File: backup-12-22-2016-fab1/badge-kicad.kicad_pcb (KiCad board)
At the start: 4 copper layers, 153.5 x 153.5 mm, 100 parts, among them J2 JTAG, P1 TM1000, P2 CONN_02X20, P3 FTDI BACKUP, P4 USB_OTG, Q1 MNBT3904, SW1 SW_PUSH, U1 WS2812B, U10 WS2812B, U11 WS2812B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

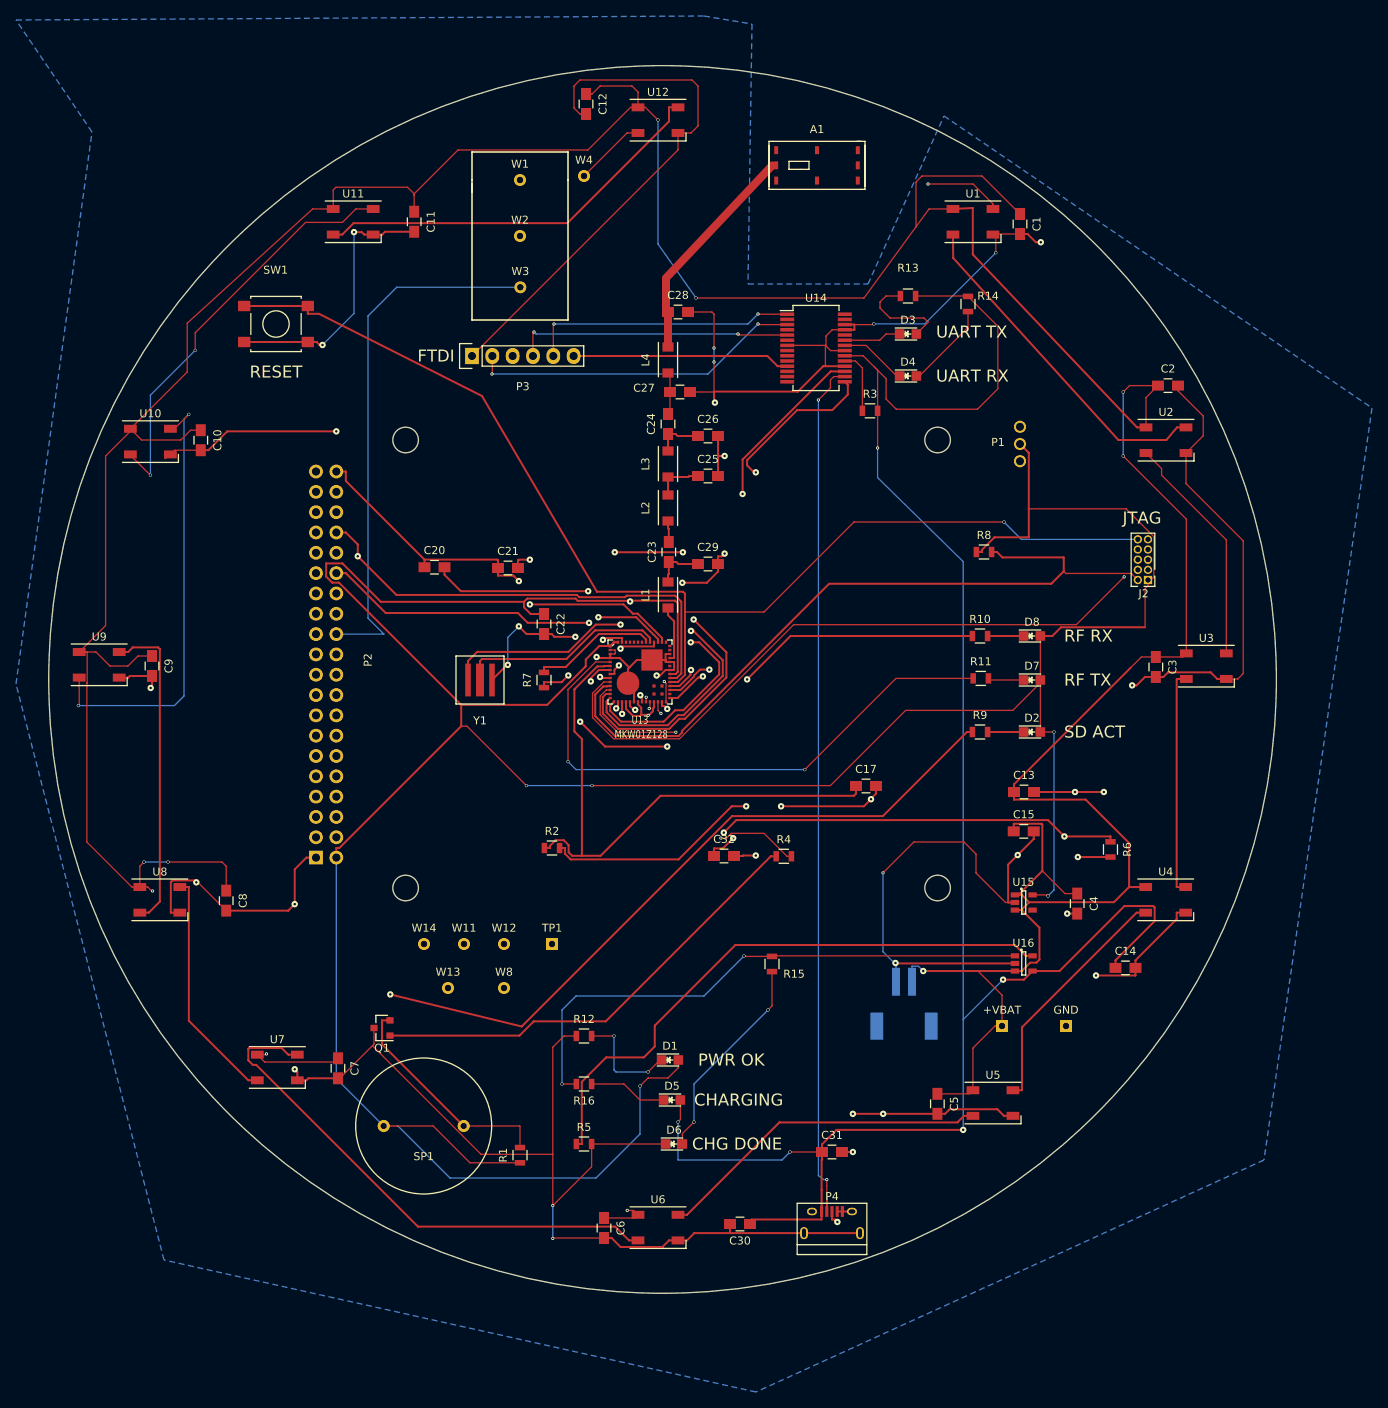
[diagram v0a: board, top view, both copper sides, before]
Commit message: new board shape, now with DAC, audio amp, and joypad
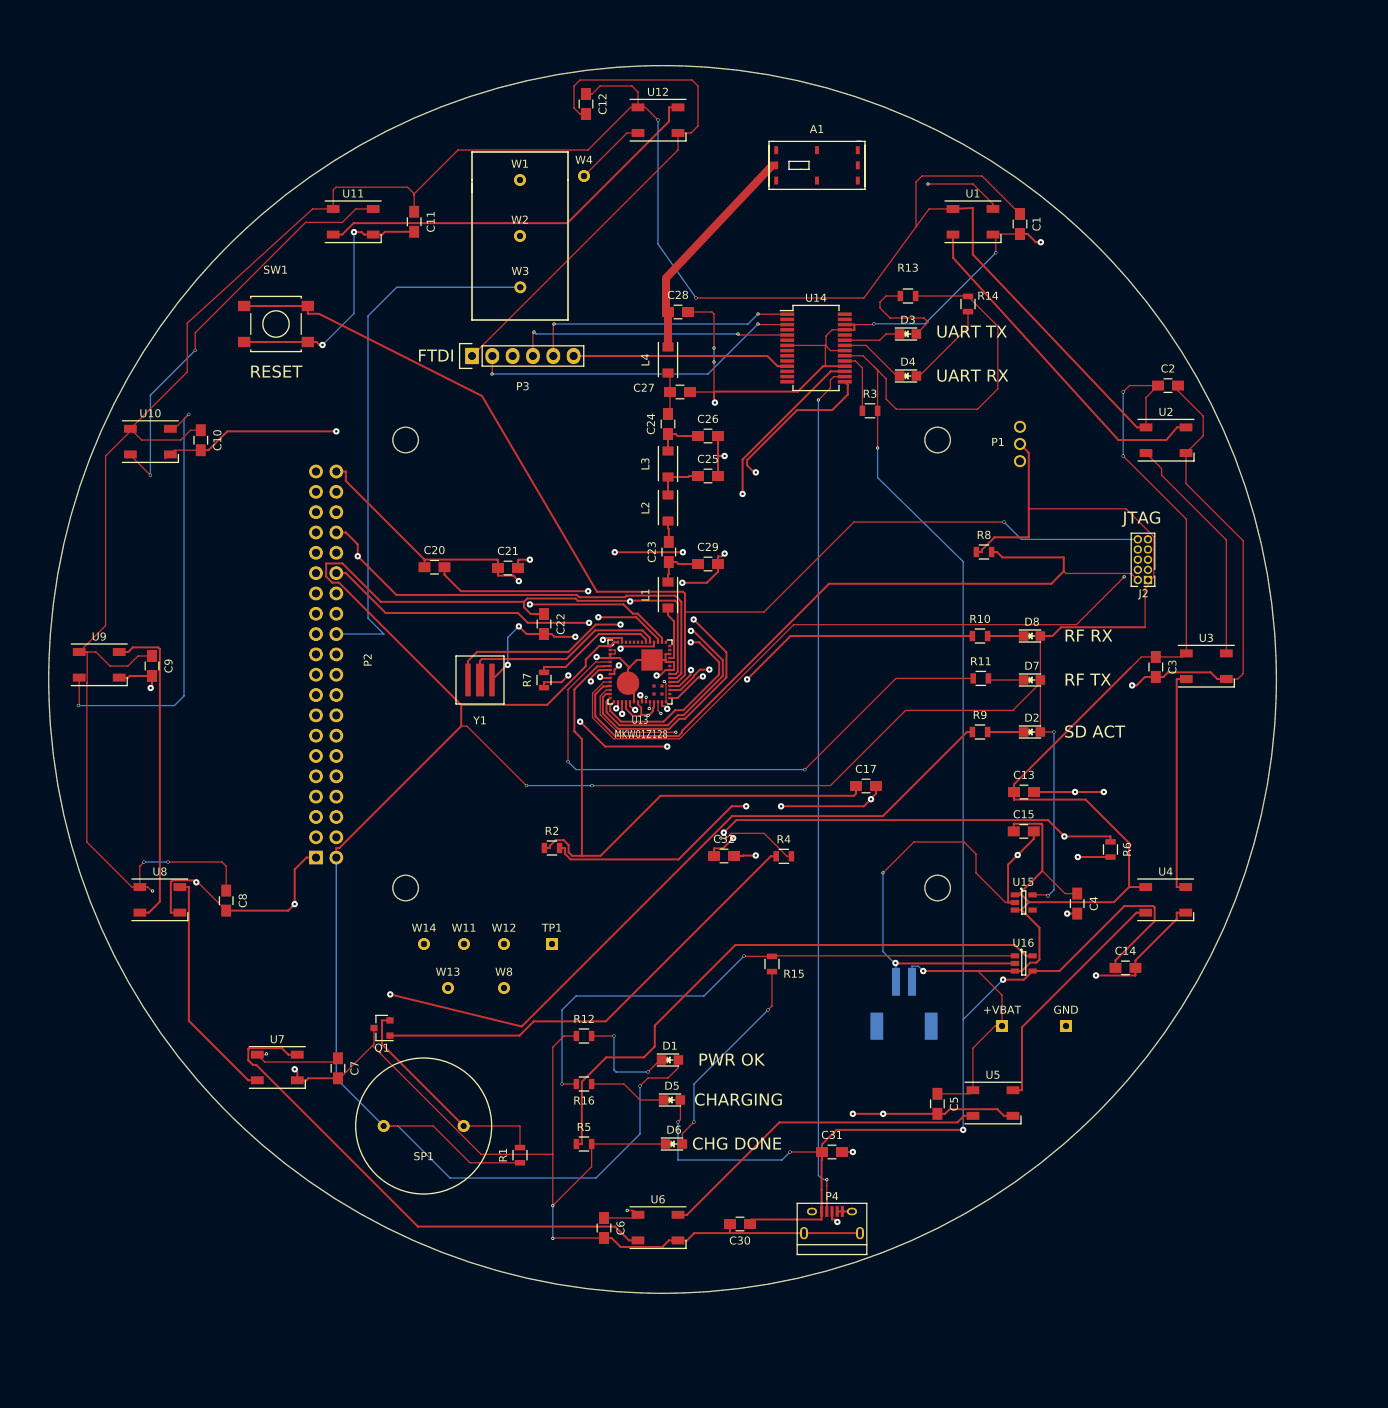
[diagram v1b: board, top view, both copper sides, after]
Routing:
- removed copper zone on B.Cu, net GND
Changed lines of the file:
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@@
   (segment (start 77.9376 147.45) (end 79.7175 145.67) (width 0.25) (layer F.Cu) (net 138))
   (segment (start 61.75 147.45) (end 77.9376 147.45) (width 0.25) (layer F.Cu) (net 138) (status 10))
-  (zone (net 1) (net_name GND) (layer B.Cu) (hatch edge 0.508)
-    (connect_pads (clearance 0.508))
-    (min_thickness 0.254)
-    (fill yes (arc_segments 32) (thermal_gap 0.508) (thermal_bridge_width 0.508))
-    (polygon
-      (pts
-        (xy 15 20.5) (xy 101 20) (xy 107 21) (xy 106.5 53.5) (xy 121.5 53.5)
-        (xy 131 32.5) (xy 184.5 69) (xy 171 163) (xy 107.5 192) (xy 33.5 175.5)
-        (xy 15 103.5) (xy 24.5 34.5)
-      )
-    )
-  )
 )
